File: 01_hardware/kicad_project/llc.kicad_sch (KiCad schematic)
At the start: 41 parts, among them J1 VIN 12-48V, Q5 NCEP068N10G, Q6 NCEP068N10G, Q7 BSC160N15NS5, Q8 BSC160N15NS5, T1 PQ2620 4:8+8, U10 UCC27211DDAR, U11 UCC27524DR

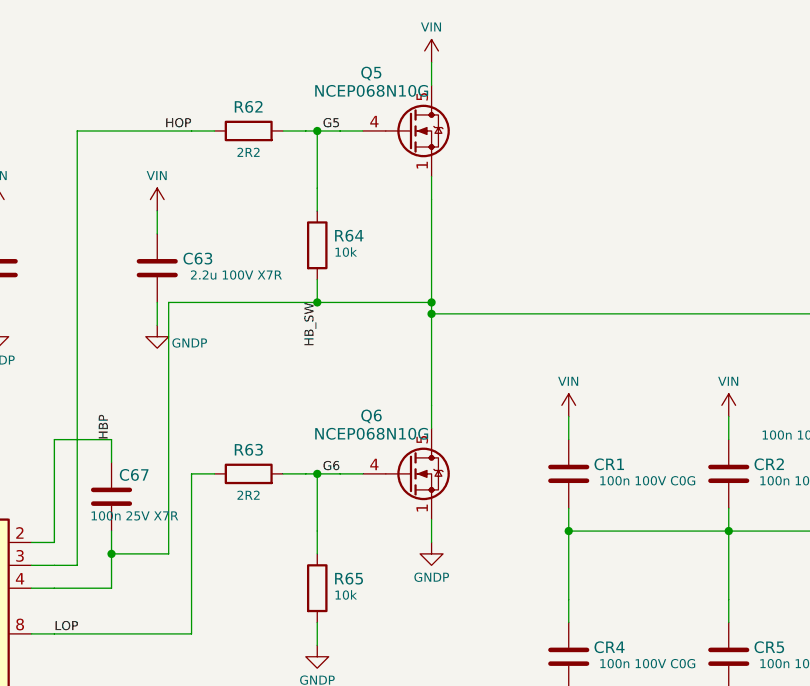
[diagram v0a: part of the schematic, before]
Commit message: Rev E2: debug-port series resistors, DRC clean (0 errors / 0 warnings)
- R123-R128 47.5 Ohm 0402 (C82290) in SWDIO, SWCLK, TP_DAC, TP_GPIO1,
  TP_GPIO2, NRST; R129 2 Ohm 0603 (C2933191) +3V3 -> J6.7 / J7 VTref
  (PROG_3V3). Placed on the MCU side of the J6/J7 branch, inserted into
  the existing traces.
- Cleared the 16 courtyard overlaps (T1/CR*/R64, T2/D8/C94/R116/C95/Q11/
  R114, C98/R122, C69/U11, C34/U1) with small moves, tracks re-attached;
  silk warnings gone. Parity 291 parts / 796 pads, 0 mismatches.
- BOMs, JLC BOM/CPL, gerbers, PDFs, EasyEDA zip, sourcing workbook,
  design notes, DRC report, README updated; scripts in 04_scripts/pcb6.

Co-Authored-By: Claude Opus 5.5 <noreply@anthropic.com>
Claude-Session: https://claude.ai/code/session_01A35wrnwFKLPSaRSxxHs471
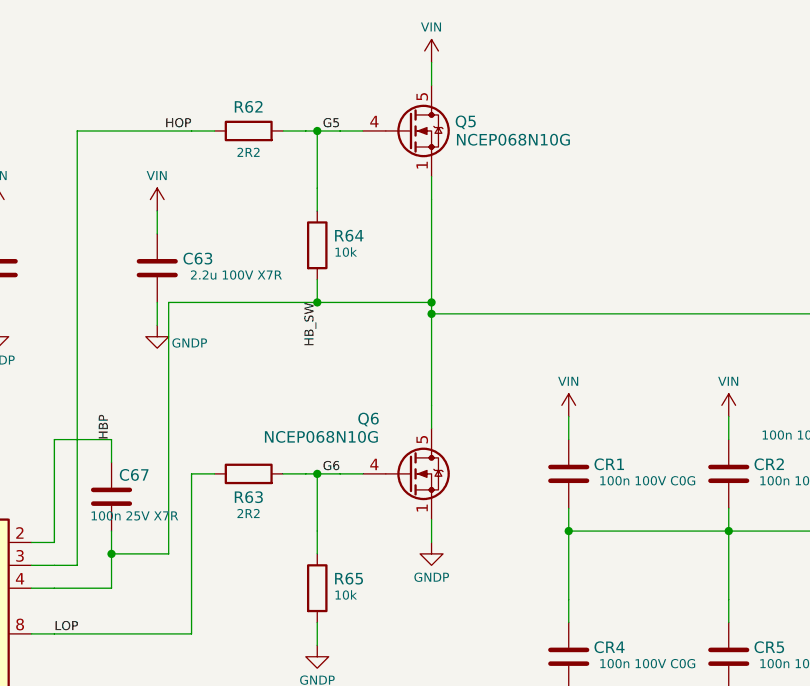
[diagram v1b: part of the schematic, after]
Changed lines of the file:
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@@
   (symbol (lib_id "Transistor_FET:BSC040N10NS5") (at 139.7 63.5 0) (unit 1)
     (in_bom yes) (on_board yes)
-    (property "Reference" "Q5" (id 0) (at 135.572 57.058 0)
-      (effects (font (size 1.27 1.27)))
-    )
-    (property "Value" "NCEP068N10G" (id 1) (at 135.572 59.09 0)
+    (property "Reference" "Q5" (id 0) (at 146.063 62.484 0)
+      (effects (font (size 1.27 1.27)))
+    )
+    (property "Value" "NCEP068N10G" (id 1) (at 151.321 64.516 0)
       (effects (font (size 1.27 1.27)))
     )
@@
   (symbol (lib_id "Transistor_FET:BSC040N10NS5") (at 139.7 101.6 0) (unit 1)
     (in_bom yes) (on_board yes)
-    (property "Reference" "Q6" (id 0) (at 135.572 95.158 0)
-      (effects (font (size 1.27 1.27)))
-    )
-    (property "Value" "NCEP068N10G" (id 1) (at 135.572 97.19 0)
+    (property "Reference" "Q6" (id 0) (at 135.242 95.504 0)
+      (effects (font (size 1.27 1.27)))
+    )
+    (property "Value" "NCEP068N10G" (id 1) (at 129.984 97.536 0)
       (effects (font (size 1.27 1.27)))
     )
@@
   (symbol (lib_id "Device:R") (at 121.92 101.6 90) (unit 1)
     (in_bom yes) (on_board yes)
-    (property "Reference" "R63" (id 0) (at 121.92 98.968 90)
-      (effects (font (size 1.27 1.27)))
-    )
-    (property "Value" "2R2" (id 1) (at 121.92 104.016 90)
-      (effects (font (size 1.0 1.0)))
-    )
+    (property "Reference" "R63" (id 0) (at 121.92 104.232 90)
+      (effects (font (size 1.27 1.27)))
+    )
+    (property "Value" "2R2" (id 1) (at 121.92 106.048 90)
+      (effects (font (size 1.0 1.0)))
+    )
